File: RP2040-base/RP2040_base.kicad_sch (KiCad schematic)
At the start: 24 parts, among them SW1 SW_Push, U1 W25Q16JV, U2 RP2040, Y2 ECS-120-8-33-JGN-TR3

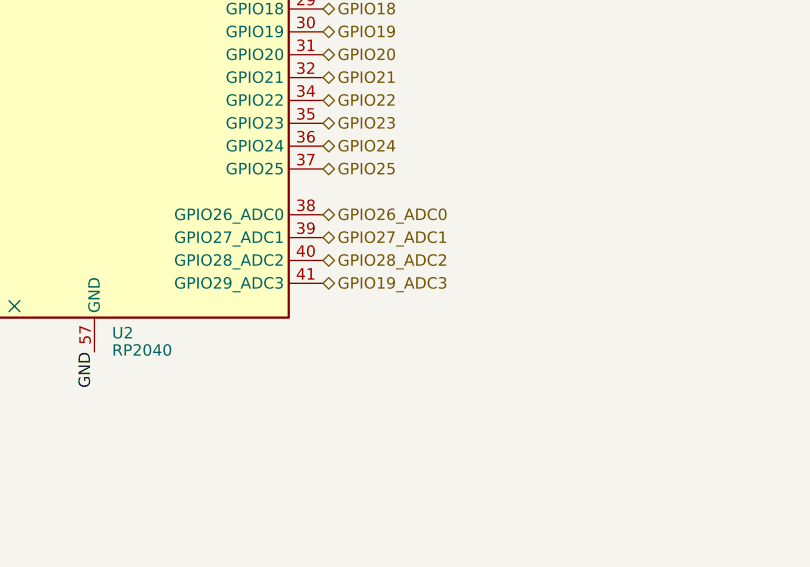
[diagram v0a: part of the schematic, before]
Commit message: Fix GPIO29_ADC3 pin name
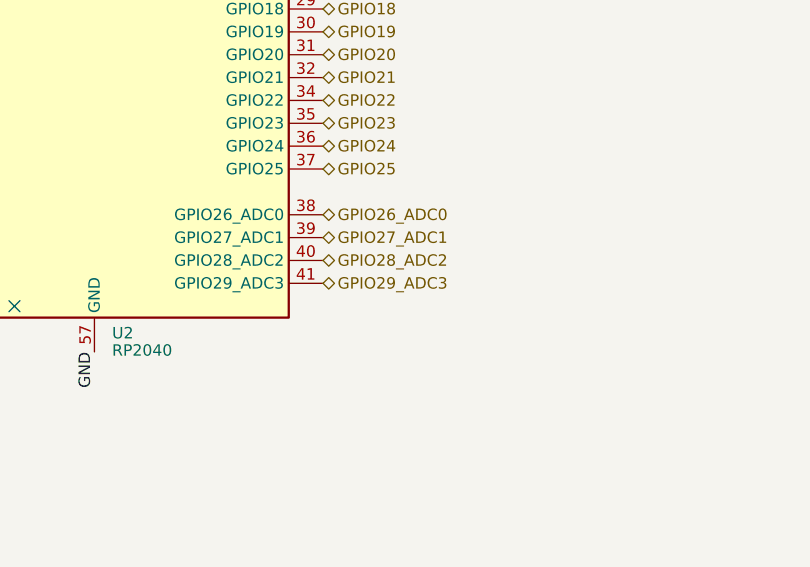
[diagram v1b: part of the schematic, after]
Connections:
- net GPIO19_ADC3 renamed GPIO29_ADC3
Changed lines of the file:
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@@
     (effects (font (size 1.27 1.27)) (justify left))
   )
-  (hierarchical_label "GPIO19_ADC3" (shape bidirectional) (at 204.47 148.59 0) (fields_autoplaced)
+  (hierarchical_label "GPIO29_ADC3" (shape bidirectional) (at 204.47 148.59 0) (fields_autoplaced)
     (effects (font (size 1.27 1.27)) (justify left))
   )

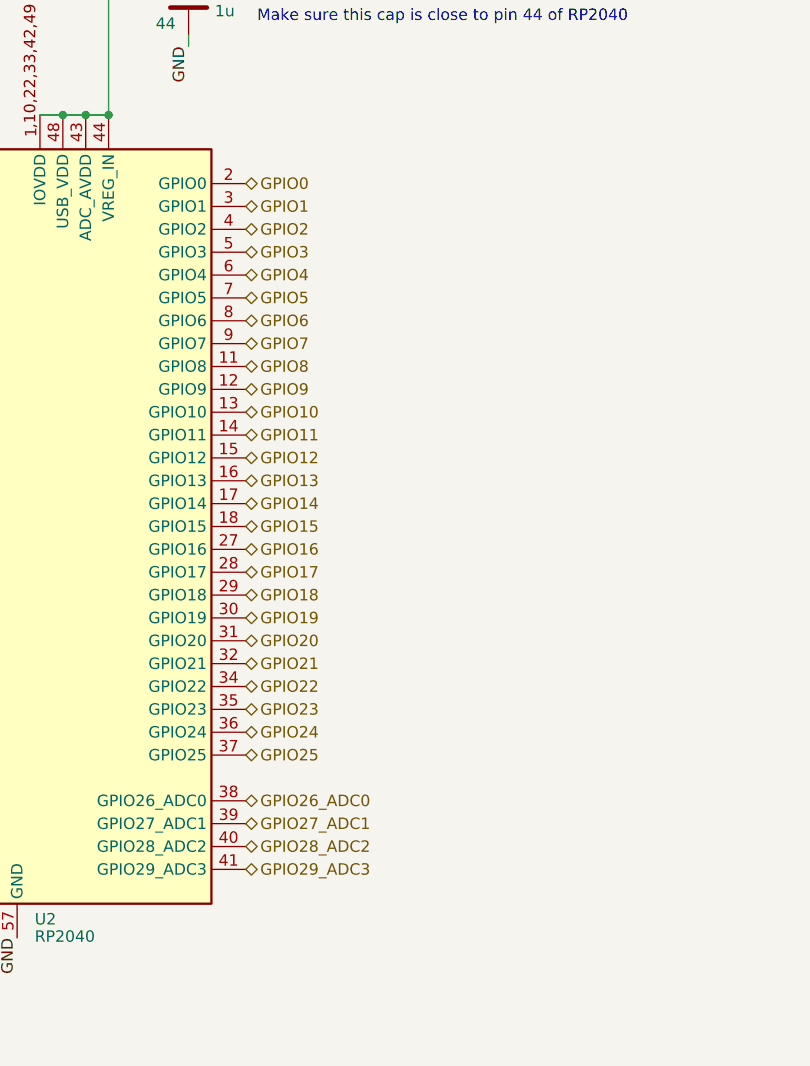
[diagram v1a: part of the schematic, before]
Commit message: Expose pins through bus instead
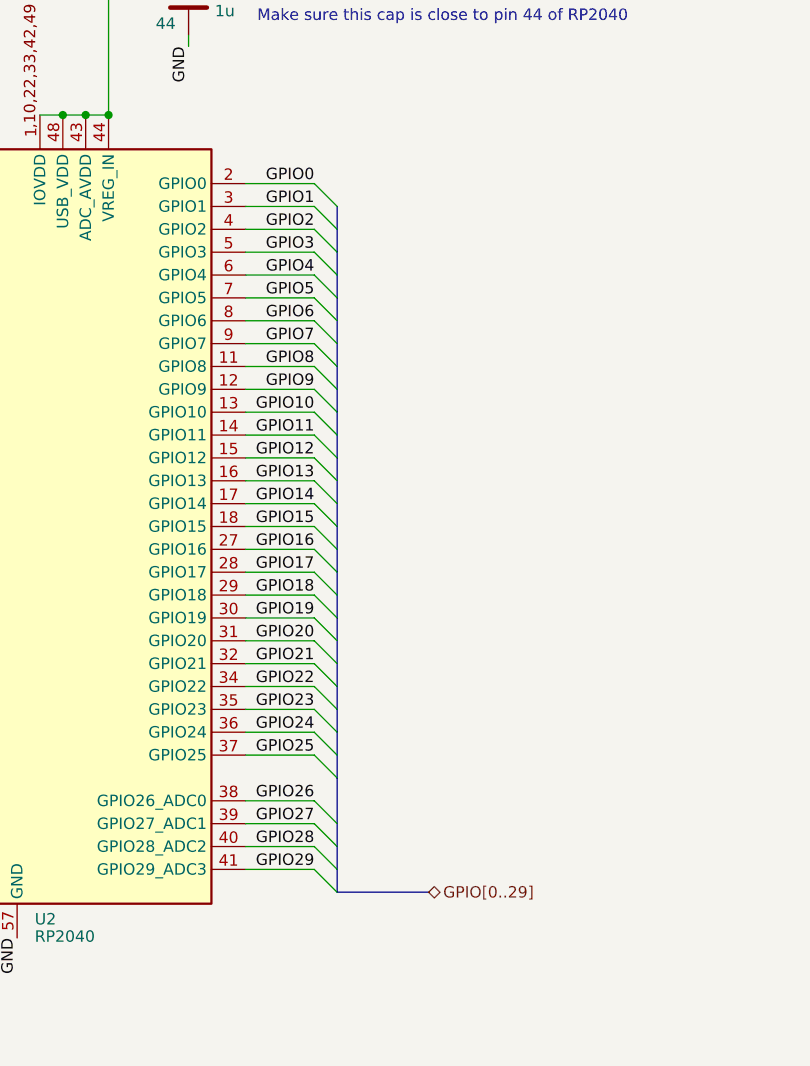
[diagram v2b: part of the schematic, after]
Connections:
- net GPIO26_ADC0 renamed GPIO26
- net GPIO27_ADC1 renamed GPIO27
- net GPIO28_ADC2 renamed GPIO28
- net GPIO29_ADC3 renamed GPIO29

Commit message: Reannotate
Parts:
- renumbered C18 to C1, C9 to C10, C6 to C11, C7 to C12, C31 to C13, C32 to C14, C29 to C15, C30 to C16, C19 to C2, C8 to C3, C5 to C4, C4 to C5, C3 to C6, C2 to C7, C1 to C8, C28 to C9, R6 to R1, R7 to R2, R10 to R3, R8 to R4, U2 to U1, U1 to U2, Y2 to Y1
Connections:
- no-connect marks 1 -> 0

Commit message: Swap crystal
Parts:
- U4: renamed from U2; value W25Q16JV -> W25QXXXJV
- Y1: value ECS-120-8-33-JGN-TR3 -> X322512MSB4SI; footprint Crystal:Crystal_SMD_EuroQuartz_MT-4Pin_3.2x2.5mm -> RP2040_base:YSX321SL, datasheet recommended measurements
- renumbered C8 to C10, C9 to C11, C10 to C12, C11 to C13, C12 to C14, C13 to C15, C14 to C16, C15 to C17, C16 to C18, C1 to C3, C2 to C4, C3 to C5, C4 to C6, C5 to C7, C6 to C8, C7 to C9, R1 to R3, R2 to R4, R3 to R5, R4 to R6, U1 to U3

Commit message: Rotate footprints to coincide with jlcpcb rotation
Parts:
- U4: footprint SOIC-8_5.275x5.275mm_P1.27mm -> RP2040_base:SOIC-8_5.275x5.275mm_P1.27mm
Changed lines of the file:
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@@
     (title "RP2040 Base")
     (date "2023-07-25")
-    (rev "0.2")
+    (rev "0.3")
     (company "https://github.com/TT-392/RP2040-base")
   )
@@
       (effects (font (size 1.27 1.27)) (justify left))
     )
-    (property "Footprint" "SOIC-8_5.275x5.275mm_P1.27mm" (at 88.9 171.45 0)
-      (effects (font (size 1.27 1.27)) hide)
-    )
+    (property "Footprint" "RP2040_base:SOIC-8_5.275x5.275mm_P1.27mm" (at 88.9 171.45 0)
+      (effects (font (size 1.27 1.27)) hide)
+    )
